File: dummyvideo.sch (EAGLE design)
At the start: 9 parts, among them IC1 NE555

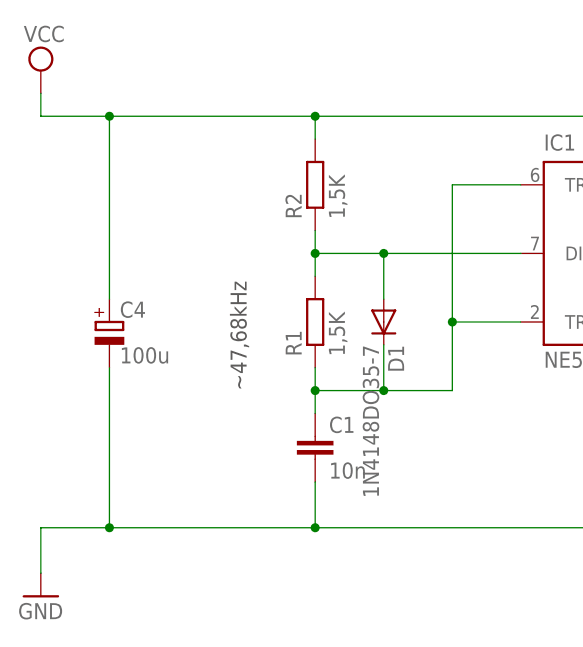
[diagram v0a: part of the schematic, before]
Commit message: Betriebs-LED eingefügt und Package des Ladekondensators
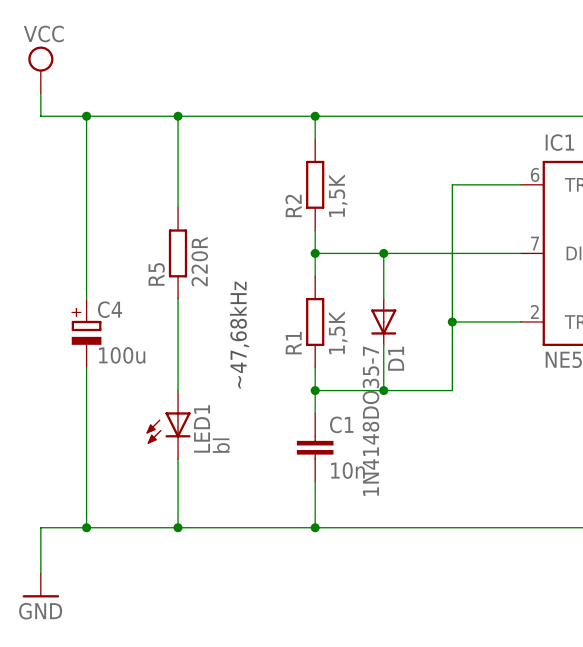
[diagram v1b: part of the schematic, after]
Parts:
- added LED1: bl, led:LED3MM
- added R5: 220R, resistor:R-EU_0207/10
- C4: device resistor:CPOL-EUE30-10AXIAL -> resistor:CPOL-EUE15-6AXIAL
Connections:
- new net N$5: LED1.A, R5.1
- net GND: now also LED1.C
- net VCC: now also R5.2
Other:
- moved on the sheet: C4
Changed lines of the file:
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@@
 <grid distance="0.1" unitdist="inch" unit="inch" style="lines" multiple="1" display="no" altdistance="0.01" altunitdist="inch" altunit="inch"/>
 <layers>
-<layer number="1" name="Top" color="4" fill="1" visible="no" active="no"/>
-<layer number="16" name="Bottom" color="1" fill="1" visible="no" active="no"/>
-<layer number="17" name="Pads" color="2" fill="1" visible="no" active="no"/>
-<layer number="18" name="Vias" color="2" fill="1" visible="no" active="no"/>
-<layer number="19" name="Unrouted" color="6" fill="1" visible="no" active="no"/>
-<layer number="20" name="Dimension" color="15" fill="1" visible="no" active="no"/>
-<layer number="21" name="tPlace" color="7" fill="1" visible="no" active="no"/>
-<layer number="22" name="bPlace" color="7" fill="1" visible="no" active="no"/>
-<layer number="23" name="tOrigins" color="15" fill="1" visible="no" active="no"/>
-<layer number="24" name="bOrigins" color="15" fill="1" visible="no" active="no"/>
-<layer number="25" name="tNames" color="7" fill="1" visible="no" active="no"/>
-<layer number="26" name="bNames" color="7" fill="1" visible="no" active="no"/>
-<layer number="27" name="tValues" color="7" fill="1" visible="no" active="no"/>
-<layer number="28" name="bValues" color="7" fill="1" visible="no" active="no"/>
+<layer number="1" name="Top" color="4" fill="1" visible="yes" active="no"/>
+<layer number="16" name="Bottom" color="1" fill="1" visible="yes" active="no"/>
+<layer number="17" name="Pads" color="2" fill="1" visible="yes" active="no"/>
+<layer number="18" name="Vias" color="2" fill="1" visible="yes" active="no"/>
+<layer number="19" name="Unrouted" color="6" fill="1" visible="yes" active="no"/>
+<layer number="20" name="Dimension" color="15" fill="1" visible="yes" active="no"/>
+<layer number="21" name="tPlace" color="7" fill="1" visible="yes" active="no"/>
+<layer number="22" name="bPlace" color="7" fill="1" visible="yes" active="no"/>
+<layer number="23" name="tOrigins" color="15" fill="1" visible="yes" active="no"/>
+<layer number="24" name="bOrigins" color="15" fill="1" visible="yes" active="no"/>
+<layer number="25" name="tNames" color="7" fill="1" visible="yes" active="no"/>
+<layer number="26" name="bNames" color="7" fill="1" visible="yes" active="no"/>
+<layer number="27" name="tValues" color="7" fill="1" visible="yes" active="no"/>
+<layer number="28" name="bValues" color="7" fill="1" visible="yes" active="no"/>
 <layer number="29" name="tStop" color="7" fill="3" visible="no" active="no"/>
 <layer number="30" name="bStop" color="7" fill="6" visible="no" active="no"/>
@@
 <layer number="35" name="tGlue" color="7" fill="4" visible="no" active="no"/>
 <layer number="36" name="bGlue" color="7" fill="5" visible="no" active="no"/>
-<layer number="37" name="tTest" color="7" fill="1" visible="no" active="no"/>
-<layer number="38" name="bTest" color="7" fill="1" visible="no" active="no"/>
+<layer number="37" name="tTest" color="7" fill="1" visible="yes" active="no"/>
+<layer number="38" name="bTest" color="7" fill="1" visible="yes" active="no"/>
 <layer number="39" name="tKeepout" color="4" fill="11" visible="no" active="no"/>
 <layer number="40" name="bKeepout" color="1" fill="11" visible="no" active="no"/>
@@
 <layer number="44" name="Drills" color="7" fill="1" visible="no" active="no"/>
 <layer number="45" name="Holes" color="7" fill="1" visible="no" active="no"/>
-<layer number="46" name="Milling" color="3" fill="1" visible="no" active="no"/>
-<layer number="47" name="Measures" color="7" fill="1" visible="no" active="no"/>
-<layer number="48" name="Document" color="7" fill="1" visible="no" active="no"/>
-<layer number="49" name="Reference" color="7" fill="1" visible="no" active="no"/>
-<layer number="51" name="tDocu" color="6" fill="1" visible="no" active="no"/>
-<layer number="52" name="bDocu" color="7" fill="1" visible="no" active="no"/>
+<layer number="46" name="Milling" color="3" fill="1" visible="yes" active="no"/>
+<layer number="47" name="Measures" color="7" fill="1" visible="yes" active="no"/>
+<layer number="48" name="Document" color="7" fill="1" visible="yes" active="no"/>
+<layer number="49" name="Reference" color="7" fill="1" visible="yes" active="no"/>
+<layer number="51" name="tDocu" color="6" fill="1" visible="yes" active="no"/>
+<layer number="52" name="bDocu" color="7" fill="1" visible="yes" active="no"/>
 <layer number="91" name="Nets" color="2" fill="1" visible="yes" active="yes"/>
 <layer number="92" name="Busses" color="1" fill="1" visible="yes" active="yes"/>
@@
 <part name="GND1" library="supply1" deviceset="GND" device=""/>
 <part name="SUPPLY1" library="supply2" deviceset="VCC" device=""/>
-<part name="C4" library="resistor" deviceset="CPOL-EU" device="E30-10AXIAL" value="100u"/>
+<part name="C4" library="resistor" deviceset="CPOL-EU" device="E15-6AXIAL" value="100u"/>
 <part name="C3" library="resistor" deviceset="C-EU" device="025-025X050" value="100n"/>
 <part name="R1" library="resistor" deviceset="R-EU_" device="0207/10" value="1,5K"/>
@@
 <part name="R3" library="resistor" deviceset="R-EU_" device="0207/10" value="4,7K"/>
 <part name="R4" library="resistor" deviceset="R-EU_" device="0207/10" value="1,5K"/>
+<part name="LED1" library="led" deviceset="LED" device="3MM" value="bl"/>
+<part name="R5" library="resistor" deviceset="R-EU_" device="0207/10" value="220R"/>
 </parts>
 <sheets>
@@
 <instance part="GND1" gate="1" x="-7.62" y="20.32"/>
 <instance part="SUPPLY1" gate="G$1" x="-7.62" y="78.74"/>
-<instance part="C4" gate="G$1" x="0" y="50.8"/>
+<instance part="C4" gate="G$1" x="-2.54" y="50.8"/>
 <instance part="C3" gate="G$1" x="76.2" y="45.72"/>
 <instance part="R1" gate="G$1" x="22.86" y="50.8" rot="R90"/>
@@
 <instance part="R3" gate="G$1" x="91.44" y="50.8" rot="R90"/>
 <instance part="R4" gate="G$1" x="91.44" y="35.56" rot="R90"/>
+<instance part="LED1" gate="G$1" x="7.62" y="40.64"/>
+<instance part="R5" gate="G$1" x="7.62" y="58.42" rot="R90"/>
 </instances>
 <busses>
@@
 <wire x1="22.86" y1="71.12" x2="22.86" y2="73.66" width="0.1524" layer="91"/>
 <wire x1="22.86" y1="73.66" x2="71.12" y2="73.66" width="0.1524" layer="91"/>
-<wire x1="22.86" y1="73.66" x2="0" y2="73.66" width="0.1524" layer="91"/>
+<wire x1="22.86" y1="73.66" x2="7.62" y2="73.66" width="0.1524" layer="91"/>
 <junction x="22.86" y="73.66"/>
 <pinref part="SUPPLY1" gate="G$1" pin="VCC"/>
-<wire x1="0" y1="73.66" x2="-7.62" y2="73.66" width="0.1524" layer="91"/>
+<wire x1="7.62" y1="73.66" x2="-2.54" y2="73.66" width="0.1524" layer="91"/>
+<wire x1="-2.54" y1="73.66" x2="-7.62" y2="73.66" width="0.1524" layer="91"/>
 <wire x1="-7.62" y1="73.66" x2="-7.62" y2="76.2" width="0.1524" layer="91"/>
 <pinref part="C4" gate="G$1" pin="+"/>
-<wire x1="0" y1="53.34" x2="0" y2="73.66" width="0.1524" layer="91"/>
-<junction x="0" y="73.66"/>
+<wire x1="-2.54" y1="53.34" x2="-2.54" y2="73.66" width="0.1524" layer="91"/>
+<junction x="-2.54" y="73.66"/>
+<pinref part="R5" gate="G$1" pin="2"/>
+<wire x1="7.62" y1="63.5" x2="7.62" y2="73.66" width="0.1524" layer="91"/>
+<junction x="7.62" y="73.66"/>
 </segment>
 </net>
@@
 <pinref part="C1" gate="G$1" pin="2"/>
 <wire x1="22.86" y1="27.94" x2="22.86" y2="33.02" width="0.1524" layer="91"/>
-<wire x1="22.86" y1="27.94" x2="0" y2="27.94" width="0.1524" layer="91"/>
+<wire x1="22.86" y1="27.94" x2="7.62" y2="27.94" width="0.1524" layer="91"/>
 <junction x="22.86" y="27.94"/>
 <pinref part="GND1" gate="1" pin="GND"/>
-<wire x1="0" y1="27.94" x2="-7.62" y2="27.94" width="0.1524" layer="91"/>
+<wire x1="7.62" y1="27.94" x2="-2.54" y2="27.94" width="0.1524" layer="91"/>
+<wire x1="-2.54" y1="27.94" x2="-7.62" y2="27.94" width="0.1524" layer="91"/>
 <wire x1="-7.62" y1="27.94" x2="-7.62" y2="22.86" width="0.1524" layer="91"/>
 <pinref part="C4" gate="G$1" pin="-"/>
-<wire x1="0" y1="45.72" x2="0" y2="27.94" width="0.1524" layer="91"/>
-<junction x="0" y="27.94"/>
+<wire x1="-2.54" y1="45.72" x2="-2.54" y2="27.94" width="0.1524" layer="91"/>
+<junction x="-2.54" y="27.94"/>
 <pinref part="C3" gate="G$1" pin="2"/>
 <wire x1="76.2" y1="40.64" x2="76.2" y2="27.94" width="0.1524" layer="91"/>
 <junction x="76.2" y="27.94"/>
+<pinref part="LED1" gate="G$1" pin="C"/>
+<wire x1="7.62" y1="35.56" x2="7.62" y2="27.94" width="0.1524" layer="91"/>
+<junction x="7.62" y="27.94"/>
 </segment>
 </net>
@@
 </segment>
 </net>
+<net name="N$5" class="0">
+<segment>
+<pinref part="R5" gate="G$1" pin="1"/>
+<pinref part="LED1" gate="G$1" pin="A"/>
+<wire x1="7.62" y1="53.34" x2="7.62" y2="43.18" width="0.1524" layer="91"/>
+</segment>
+</net>

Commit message: erstes Board-Layout
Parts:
- added JP1: (no value), jumper:JP1E
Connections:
- net GND: now also JP1.2
- net OUT: now also JP1.1
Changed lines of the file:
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@@
 <part name="LED1" library="led" deviceset="LED" device="3MM" value="bl"/>
 <part name="R5" library="resistor" deviceset="R-EU_" device="0207/10" value="220R"/>
+<part name="JP1" library="jumper" deviceset="JP1E" device=""/>
 </parts>
 <sheets>
@@
 <instance part="LED1" gate="G$1" x="7.62" y="40.64"/>
 <instance part="R5" gate="G$1" x="7.62" y="58.42" rot="R90"/>
+<instance part="JP1" gate="A" x="116.84" y="43.18" rot="R270"/>
 </instances>
 <busses>
@@
 <wire x1="7.62" y1="35.56" x2="7.62" y2="27.94" width="0.1524" layer="91"/>
 <junction x="7.62" y="27.94"/>
+<pinref part="JP1" gate="A" pin="2"/>
+<wire x1="114.3" y1="40.64" x2="111.76" y2="40.64" width="0.1524" layer="91"/>
+<wire x1="111.76" y1="40.64" x2="111.76" y2="27.94" width="0.1524" layer="91"/>
+<wire x1="111.76" y1="27.94" x2="91.44" y2="27.94" width="0.1524" layer="91"/>
+<junction x="91.44" y="27.94"/>
 </segment>
 </net>
@@
 <wire x1="91.44" y1="45.72" x2="91.44" y2="43.18" width="0.1524" layer="91"/>
 <wire x1="91.44" y1="43.18" x2="91.44" y2="40.64" width="0.1524" layer="91"/>
-<wire x1="91.44" y1="43.18" x2="101.6" y2="43.18" width="0.1524" layer="91"/>
 <junction x="91.44" y="43.18"/>
 <label x="104.14" y="43.18" size="1.778" layer="95"/>
+<pinref part="JP1" gate="A" pin="1"/>
+<wire x1="91.44" y1="43.18" x2="114.3" y2="43.18" width="0.1524" layer="91"/>
 </segment>
 </net>
